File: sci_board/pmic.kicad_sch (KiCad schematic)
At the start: 24 parts, among them J1 Conn_01x03_Pin, U1 STM32L496VGTx

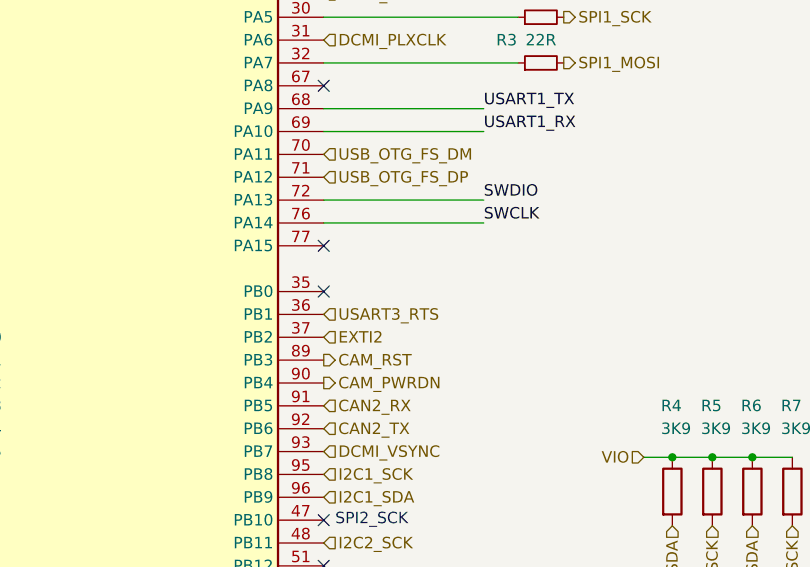
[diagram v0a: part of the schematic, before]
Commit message: cleanup around watchdog, remove TPs
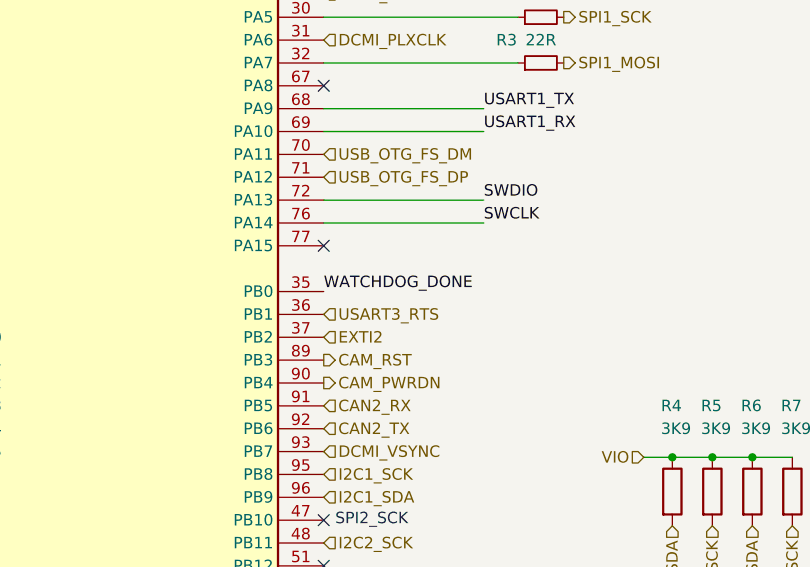
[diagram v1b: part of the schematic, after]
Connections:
- net WATCHDOG_DONE: now also U1.35 (PB0)
- no-connect marks 11 -> 10
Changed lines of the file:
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@@
 		(at 158.75 151.13)
-	)
-	(no_connect
-		(at 158.75 100.33)
 	)
 	(wire
@@
 		)
 	)
+	(label "WATCHDOG_DONE"
+		(at 158.75 100.33 0)
+		(fields_autoplaced yes)
+		(effects
+			(font
+				(size 1.27 1.27)
+			)
+			(justify left bottom)
+		)
+	)

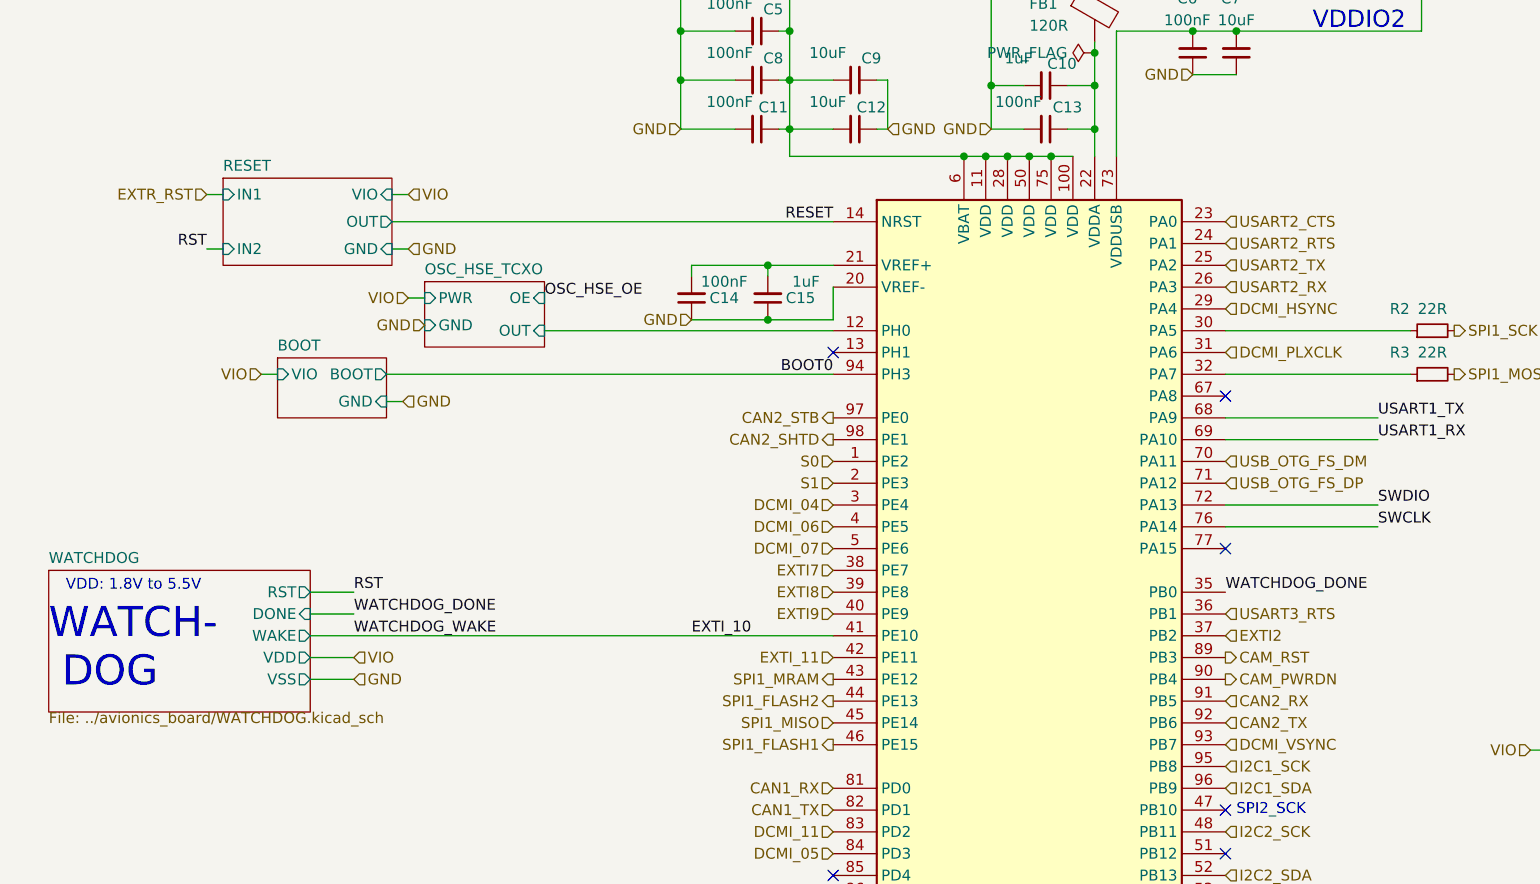
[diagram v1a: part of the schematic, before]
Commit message: add SPI CS and MISO pullups and terminations, remove WD from SCI
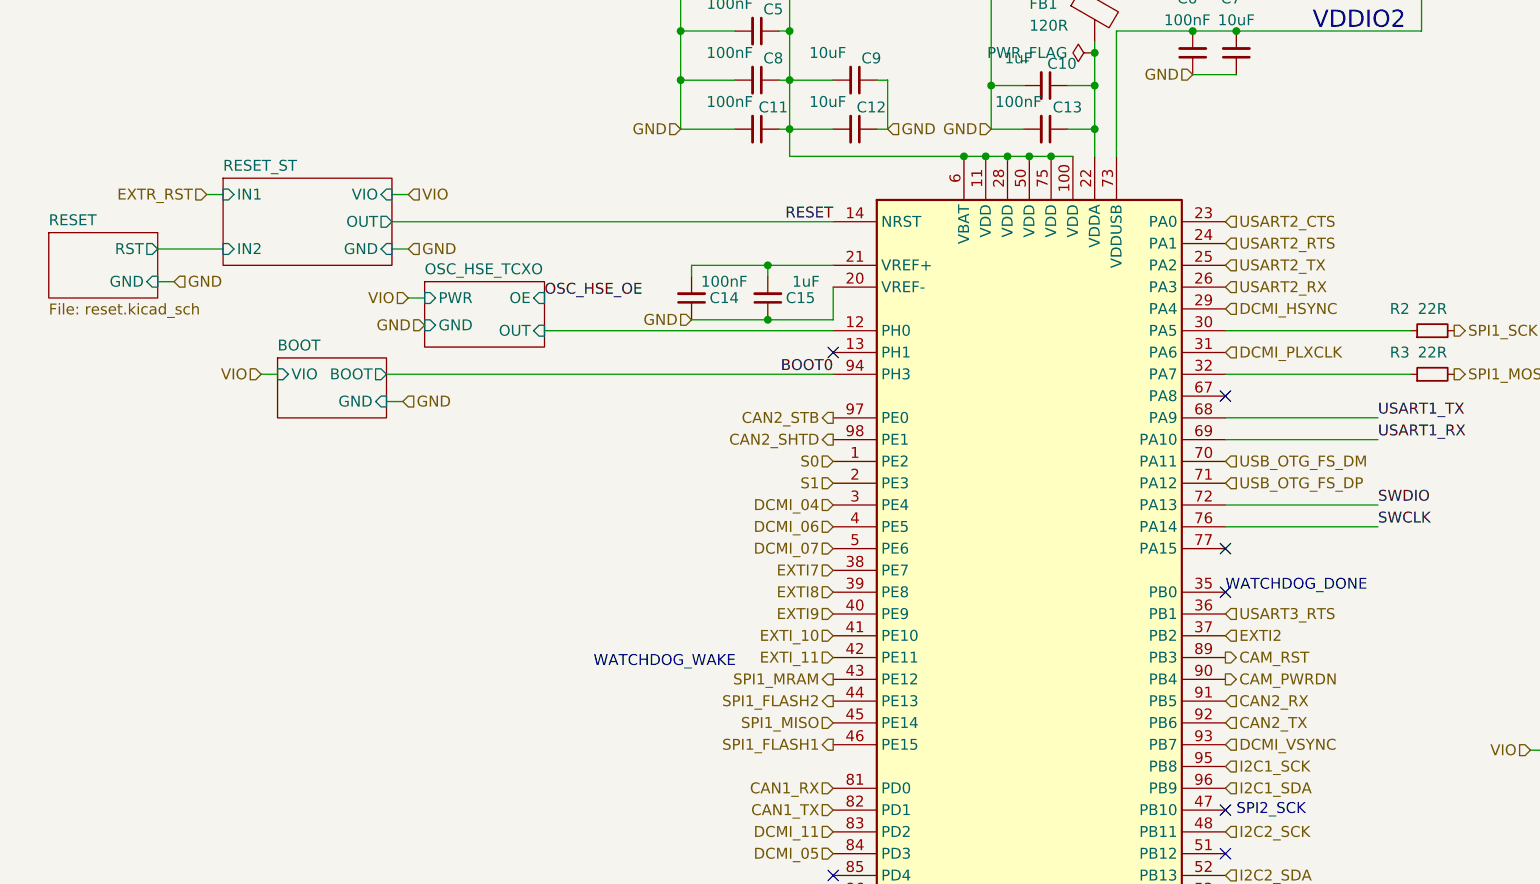
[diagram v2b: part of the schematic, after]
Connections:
- net WATCHDOG_DONE: no longer names the net of U1.35 (PB0)
- no-connect marks 10 -> 11
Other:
- removed sheet WATCHDOG
- added sheet RESET_ST (../avionics_board/schmitt_trigger.kicad_sch)
- sheet RESET: file ../avionics_board/schmitt_trigger.kicad_sch -> reset.kicad_sch
- sheet RESET ports: added RST; removed IN1, IN2, OUT, VIO
- note added: "WATCHDOG_DONE"
- note added: "WATCHDOG_WAKE"
- note removed: "VDD: 1.8V to 5.5V"
- note removed: "WATCH- DOG"

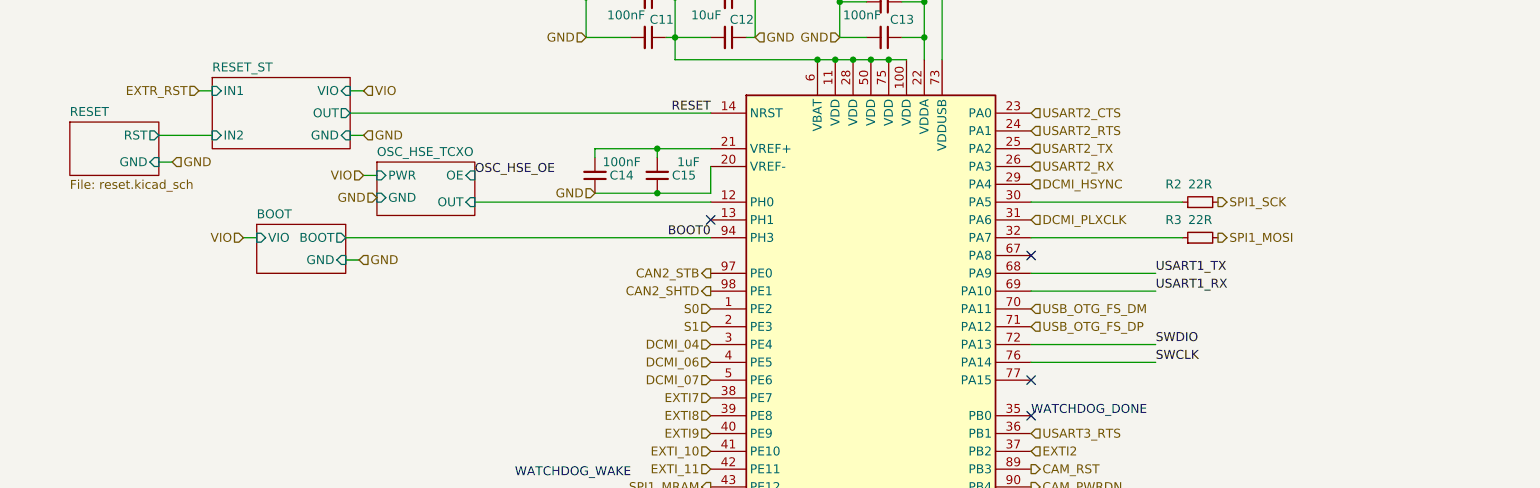
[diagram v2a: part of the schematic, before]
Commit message: tweaking SCI and AUX for production, using common sheets as much as possible
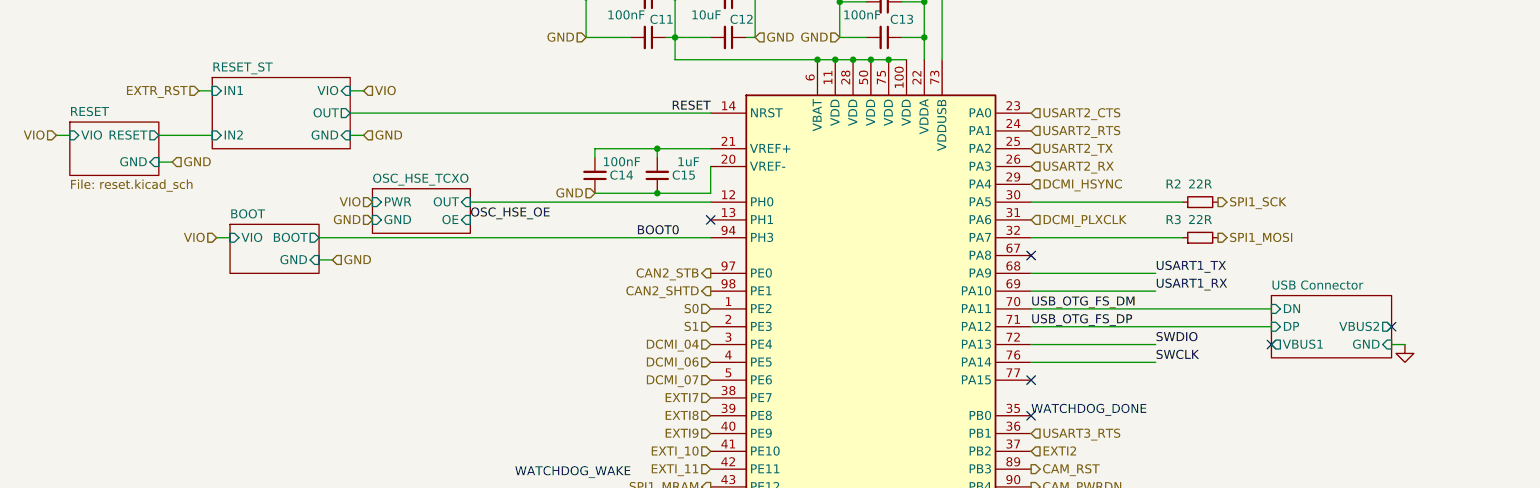
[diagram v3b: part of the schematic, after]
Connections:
- no-connect marks 11 -> 13
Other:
- added sheet USB Connector (../avionics_board/USB.kicad_sch)
- sheet RESET ports: added RESET, VIO; removed RST

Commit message: clenup BOM for SCI and AUX
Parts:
- J1: Manufacturer (none) -> generic; Part Number (none) -> generic; now fitted
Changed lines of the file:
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@@
 	)
 	(no_connect
-		(at 193.04 90.17)
+		(at 210.185 85.09)
 	)
 	(no_connect
@@
 		(in_bom yes)
 		(on_board yes)
-		(dnp yes)
+		(dnp no)
 		(fields_autoplaced yes)
 		(property "Reference" "J1"
@@
 			)
 		)
+		(property "Manufacturer" "generic"
+			(at 248.92 100.965 0)
+			(effects
+				(font
+					(size 1.27 1.27)
+				)
+				(hide yes)
+			)
+		)
+		(property "Part Number" "generic"
+			(at 248.92 100.965 0)
+			(effects
+				(font
+					(size 1.27 1.27)
+				)
+				(hide yes)
+			)
+		)
 		(pin "1"
 		)
@@
 		)
 		(pin "VBUS1" output
-			(at 193.04 90.17 180)
+			(at 210.185 85.09 0)
 			(effects
 				(font
 					(size 1.27 1.27)
 				)
-				(justify left)
+				(justify right)
 			)
 		)

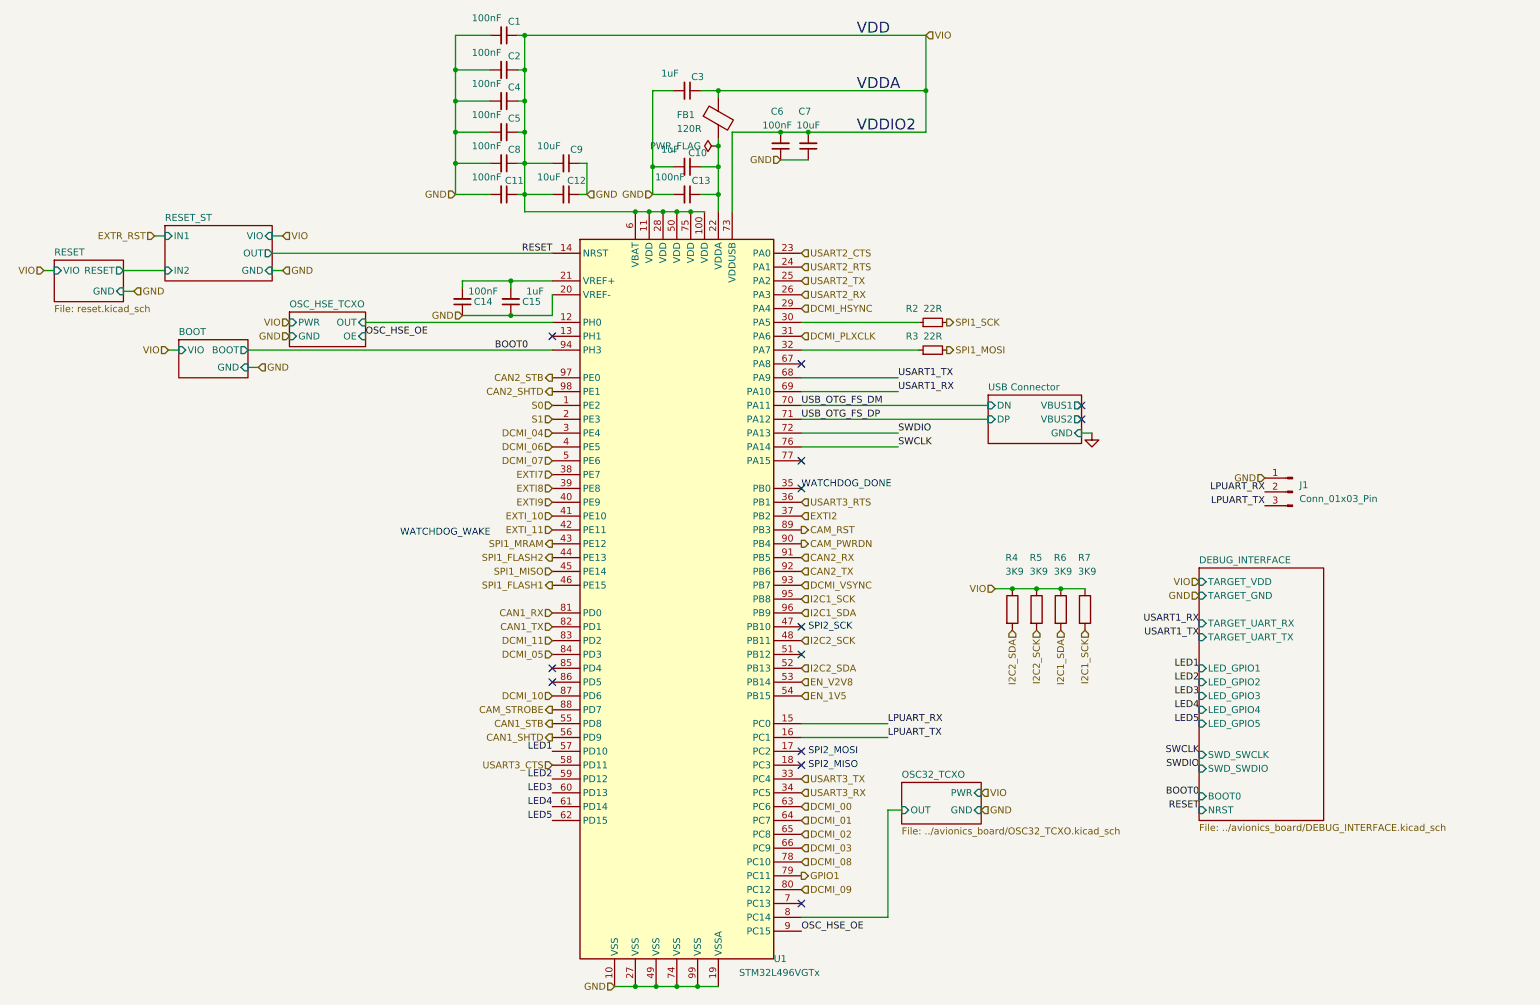
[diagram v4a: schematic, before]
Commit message: cleaning up bom: remove main camera port since it has not pullups and capacitors, correcting some errors in camera switch
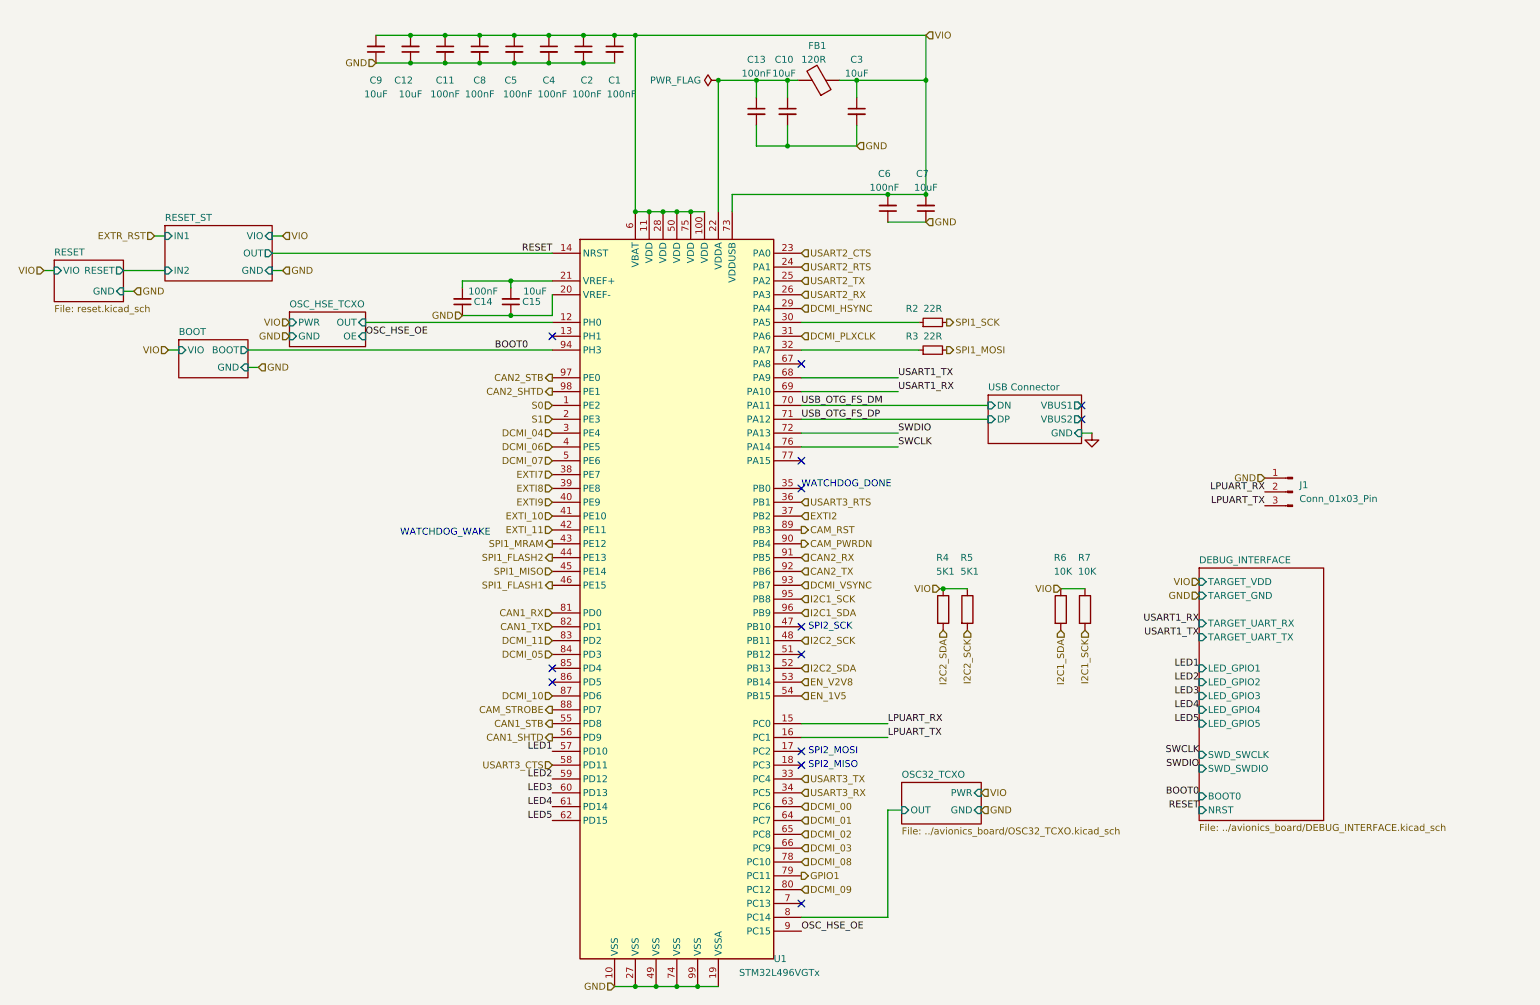
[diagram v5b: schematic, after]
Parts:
- C10, C15, C3: value 1uF -> 10uF; Part Number GRM188R61C105KA12D -> GRM188R61E106KA73D; Voltage 16 -> 25
- R4, R5: value 3K9 -> 5K1; Part Number RC0402FR-073K9L -> RC0402FR-075K1L
- R6, R7: value 3K9 -> 10K; Part Number RC0402FR-073K9L -> RC0402FR-0710KL
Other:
- note removed: "VDD"
- note removed: "VDDA"
- note removed: "VDDIO2"
- moved on the sheet: C1, C10, C11, C12, C13, C2, C3, C4, C5, C6, C7, C8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
